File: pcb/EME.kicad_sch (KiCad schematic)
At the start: 42 parts, among them J1 BMP180, J10 INPUT ONLY, J11 UART0, J12 SPI_CONN, J13 UART0, J2 ReedSwitchX8, J3 SS41, J5 PanelSolar, J6 BH1750, J7 DHT22, J8 Baterias, J9 Jumper, U1 LM78M05_TO220, U5 TL082

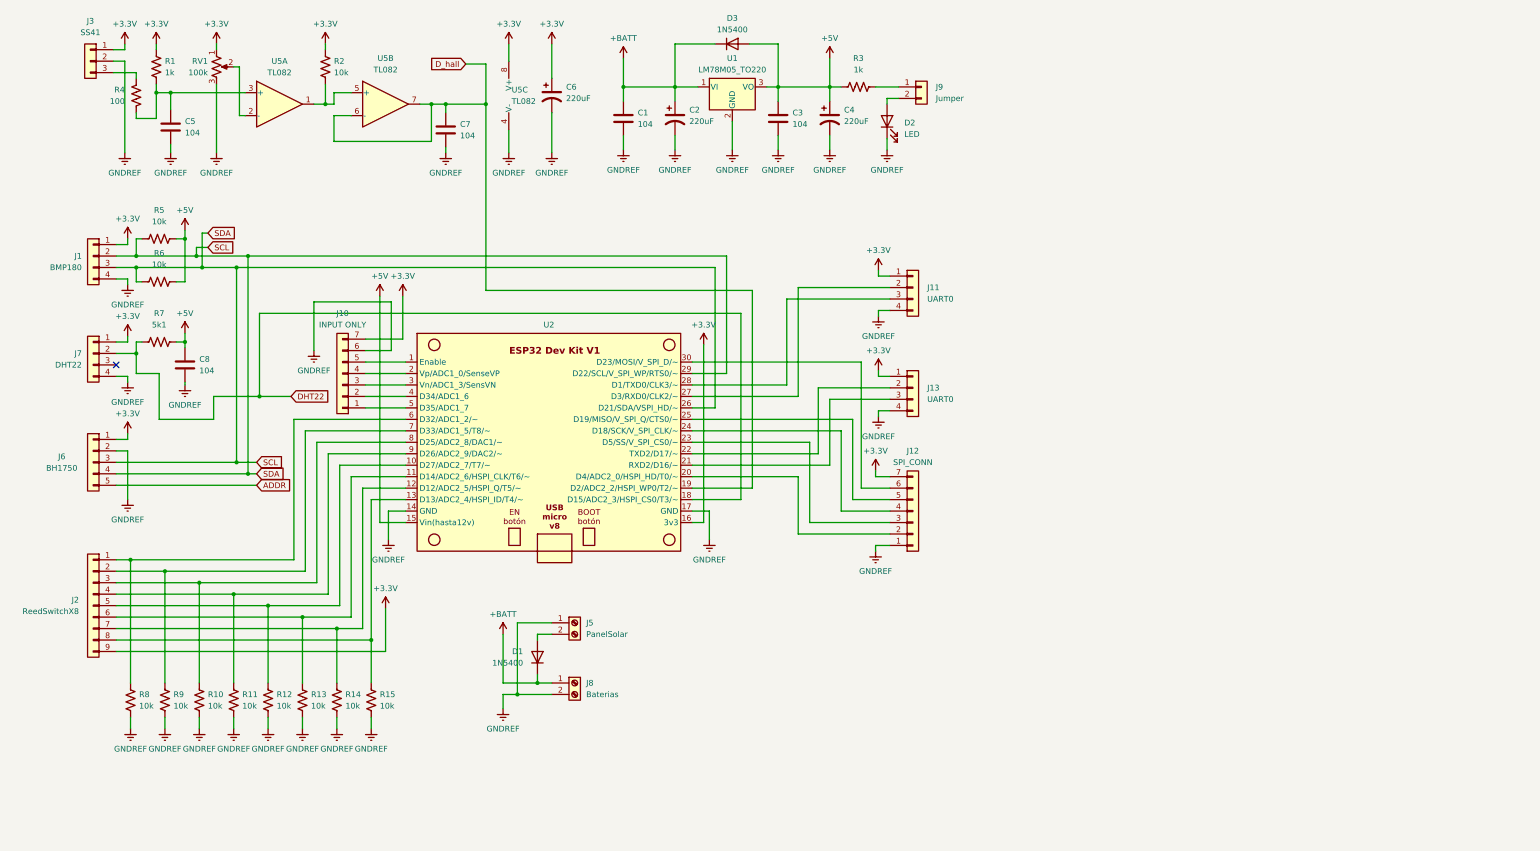
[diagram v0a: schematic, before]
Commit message: se agregaron ejemplos de los sensores y actualizo la PCB
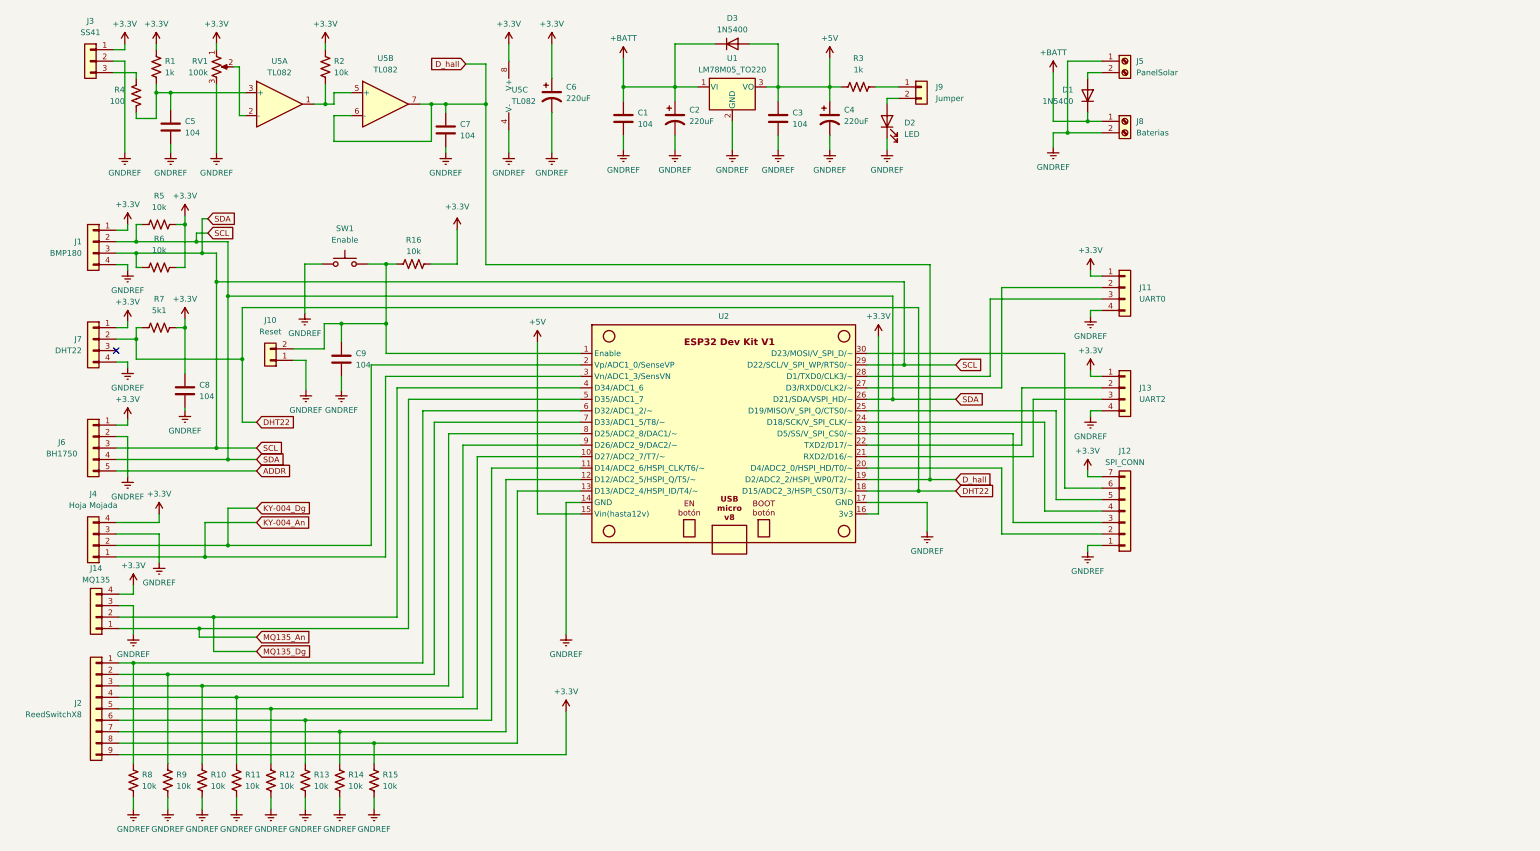
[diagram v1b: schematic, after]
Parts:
- removed J10: INPUT ONLY, Connector_PinHeader_2.54mm:PinHeader_1x07_P2.54mm_Vertical, symbol Connector_Generic:Conn_01x07
- added C9: 104, Capacitor_THT:C_Disc_D4.3mm_W1.9mm_P5.00mm, symbol Device:C
- added J10: Reset, Connector_PinHeader_2.54mm:PinHeader_1x02_P2.54mm_Vertical, symbol Connector_Generic:Conn_01x02
- added J14: MQ135, Connector_PinHeader_2.54mm:PinHeader_1x04_P2.54mm_Vertical, symbol Connector_Generic:Conn_01x04
- added J4: Hoja Mojada, Connector_PinHeader_2.54mm:PinHeader_1x04_P2.54mm_Vertical, symbol Connector_Generic:Conn_01x04
- added R16: 10k, Resistor_THT:R_Axial_DIN0207_L6.3mm_D2.5mm_P10.16mm_Horizontal, symbol Device:R_US
- added SW1: Enable, Button_Switch_THT:SW_PUSH_6mm_H8mm, symbol Switch:SW_Push
- J13: value UART0 -> UART2
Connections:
- net +3.3V: now also C8.1, R5.2, R6.2, R7.2, J14.4 (Pin_4), J4.4 (Pin_4), R16.1
- net +5V: no longer C8.1, R5.2, R6.2, R7.2
- net GNDREF: now also C9.2, J10.1 (Pin_1), J14.3 (Pin_3), J4.3 (Pin_3), SW1.1
- net at U2.1 (Enable): now also C9.1, J10.2 (Pin_2), R16.2, SW1.2
- net KY-004_Dg: now reaches U2.2 (Vp/ADC1_0/SenseVP)
- net KY-004_Dg: now also J4.2 (Pin_2)
- net KY-004_An: now reaches U2.3 (Vn/ADC1_3/SensVN)
- net KY-004_An: now also J4.1 (Pin_1)
- net MQ135_Dg: now reaches U2.4 (D34/ADC1_6)
- net MQ135_Dg: now also J14.2 (Pin_2)
- net MQ135_An: now reaches U2.5 (D35/ADC1_7)
- net MQ135_An: now also J14.1 (Pin_1)
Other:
- company: (none) -> ETec UM (Escuela Técnica de la Universidad de Mendoza)
- title: (none) -> Main Board EME (Estación Meteorológica Estática)
- moved on the sheet: C8, D1, J1, J11, J12, J13, J2, J5, J6, J7, J8, R10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

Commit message: Se armó diseño de PCB y se decoró esquemático
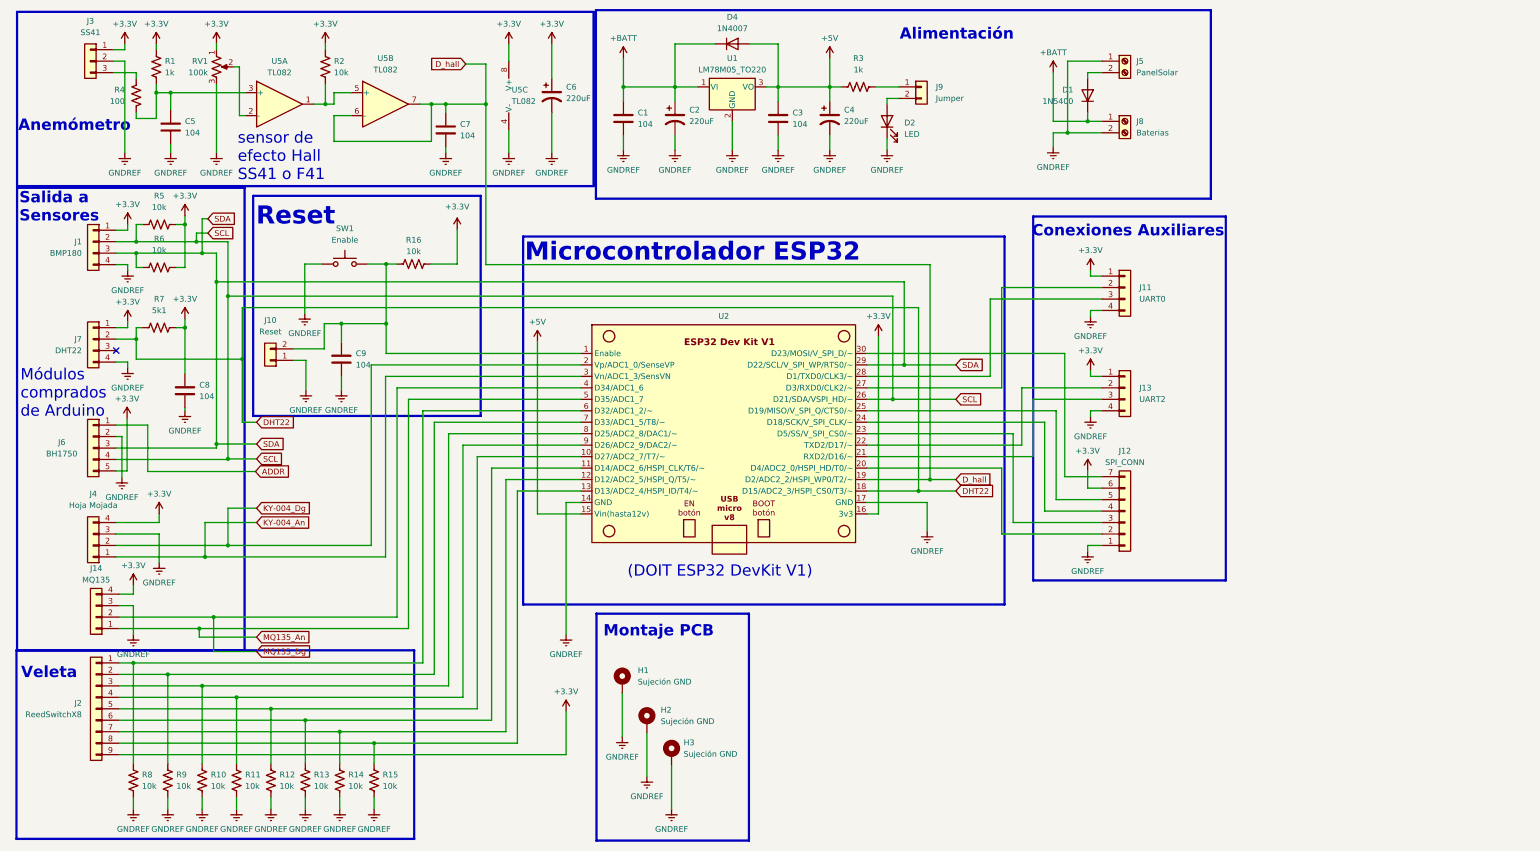
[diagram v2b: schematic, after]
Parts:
- removed D3: 1N5400, Diode_THT:D_DO-201AD_P15.24mm_Horizontal, symbol Diode:1N5400
- added D4: 1N4007, Diode_THT:D_DO-41_SOD81_P10.16mm_Horizontal, symbol Diode:1N4007
- added H1, H2, H3: Sujeción GND, MountingHole:MountingHole_3.2mm_M3_Pad_Via, symbol Mechanical:MountingHole_Pad_MP
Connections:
- net +3.3V: now also J12.6 (Pin_6), J6.5 (Pin_5); no longer J12.7 (Pin_7), J6.1 (Pin_1)
- net +5V: now also D4.2 (A)
- net +BATT: now also D4.1 (K)
- net ADDR: now also J6.1 (Pin_1); no longer J6.5 (Pin_5)
- net GNDREF: now also H1.MP, H2.MP, H3.MP
- net SCL: no longer J1.3 (Pin_3), J6.3 (Pin_3), R6.1, U2.29 (D22/SCL/V_SPI_WP/RTS0/~)
- net at U2.30 (D23/MOSI/V_SPI_D/~): now also J12.7 (Pin_7); no longer J12.6 (Pin_6)
- new net SDA: J1.3 (Pin_3), J6.3 (Pin_3), R6.1, U2.29 (D22/SCL/V_SPI_WP/RTS0/~)
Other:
- note added: "(DOIT ESP32 DevKit V1)"
- note added: "Alimentación"
- note added: "Anemómetro"
- note added: "Conexiones Auxiliares"
- note added: "Microcontrolador ESP32"
- note added: "Montaje PCB"
- note added: "Módulos comprados de Arduino"
- note added: "Reset"
- note added: "Salida a Sensores"
- note added: "Veleta"
- note added: "sensor de efecto Hall SS41 o F41"
- company: ETec UM (Escuela Técnica de la Universidad de Mendoza) -> ETec UM (Escuela Técnica de la Universidad de Mendoza).

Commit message: Add files via upload
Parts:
- removed J2: ReedSwitchX8, Connector_PinHeader_2.54mm:PinHeader_1x09_P2.54mm_Vertical, symbol Connector_Generic:Conn_01x09
- removed R10, R11, R12, R13, R14, R15, R8, R9: 10k, Resistor_THT:R_Axial_DIN0207_L6.3mm_D2.5mm_P10.16mm_Horizontal, symbol Device:R_US
- added J15: AS5600, Connector_PinHeader_2.54mm:PinHeader_1x05_P2.54mm_Vertical, symbol Connector_Generic:Conn_01x05
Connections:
- net +3.3V: now also J15.4 (Pin_4)
- net GNDREF: now also J15.5 (Pin_5)
- net SCL: now also J1.3 (Pin_3), J6.3 (Pin_3), R6.1, U2.29 (D22/SCL/V_SPI_WP/RTS0/~), J15.3 (Pin_3); no longer J1.2 (Pin_2), J6.4 (Pin_4), R5.1, U2.26 (D21/SDA/VSPI_HD/~)
- net SDA: now also J1.2 (Pin_2), J6.4 (Pin_4), R5.1, U2.26 (D21/SDA/VSPI_HD/~), J15.2 (Pin_2); no longer J1.3 (Pin_3), J6.3 (Pin_3), R6.1, U2.29 (D22/SCL/V_SPI_WP/RTS0/~)
- net at U2.6 (D32/ADC1_2/~): now also J15.1 (Pin_1)
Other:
- moved on the sheet: C1, C2, C3, C4, C5, C6, C7, C9, D1, D2, D4, H1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

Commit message: se actualizó la PCB
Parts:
- removed J11: UART0, Connector_PinHeader_2.54mm:PinHeader_1x04_P2.54mm_Vertical, symbol Connector_Generic:Conn_01x04
- removed J13: UART2, Connector_PinHeader_2.54mm:PinHeader_1x04_P2.54mm_Vertical, symbol Connector_Generic:Conn_01x04
- removed J15: AS5600, Connector_PinHeader_2.54mm:PinHeader_1x05_P2.54mm_Vertical, symbol Connector_Generic:Conn_01x05
- added D3: LED, LED_THT:LED_D5.0mm_Clear, symbol Device:LED
- added H4: Sujeción, MountingHole:MountingHole_3.2mm_M3_Pad_Via, symbol Mechanical:MountingHole_Pad_MP
- added J11: UART2, Connector_PinHeader_2.54mm:PinHeader_1x05_P2.54mm_Vertical, symbol Connector_Generic:Conn_01x05
- added J13: UART0, Connector_PinHeader_2.54mm:PinHeader_1x05_P2.54mm_Vertical, symbol Connector_Generic:Conn_01x05
- added J16: OUT, Connector_PinHeader_2.54mm:PinHeader_1x03_P2.54mm_Vertical, symbol Connector_Generic:Conn_01x03
- added J17: OE, Connector_PinHeader_2.54mm:PinHeader_1x03_P2.54mm_Vertical, symbol Connector_Generic:Conn_01x03
- added J18: GPIO's, Connector_PinHeader_2.54mm:PinHeader_1x05_P2.54mm_Vertical, symbol Connector_Generic:Conn_01x05
- added J19: I2C, Connector_PinHeader_2.54mm:PinHeader_1x05_P2.54mm_Vertical, symbol Connector_Generic:Conn_01x05
- added J2: ReedSwitchX8, Connector_PinHeader_2.54mm:PinHeader_1x09_P2.54mm_Vertical, symbol Connector_Generic:Conn_01x09
- added J20: Jumper, Connector_PinHeader_2.54mm:PinHeader_1x02_P2.54mm_Vertical, symbol Connector_Generic:Conn_01x02
- added Q1, Q2: IRF540N, Package_TO_SOT_THT:TO-220-3_Vertical, symbol Transistor_FET:IRF540N
- added R10, R11, R12, R13, R14, R15, R8, R9: 10k, Resistor_THT:R_Axial_DIN0207_L6.3mm_D2.5mm_P10.16mm_Horizontal, symbol Device:R_US
- added R17, R20, R24: 1k, Resistor_THT:R_Axial_DIN0207_L6.3mm_D2.5mm_P10.16mm_Horizontal, symbol Device:R_US
- added R18, R19, R21, R22, R23: 4k7, Resistor_THT:R_Axial_DIN0207_L6.3mm_D2.5mm_P10.16mm_Horizontal, symbol Device:R_US
- added U3: 74HC251, Package_DIP:DIP-16_W7.62mm_LongPads, symbol Connector_Generic:Conn_02x08_Counter_Clockwise
- H1, H2, H3: value Sujeción GND -> Sujeción
- J5: footprint TerminalBlock_Phoenix:TerminalBlock_Phoenix_MPT-0,5-2-2.54_1x02_P2.54mm_Horizontal -> TerminalBlock_Phoenix:TerminalBlock_Phoenix_PT-1,5-2-3.5-H_1x02_P3.50mm_Horizontal
- J8: footprint TerminalBlock_Phoenix:TerminalBlock_Phoenix_MPT-0,5-2-2.54_1x02_P2.54mm_Horizontal -> TerminalBlock_Phoenix:TerminalBlock_Phoenix_PT-1,5-2-5.0-H_1x02_P5.00mm_Horizontal
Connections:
- net +3.3V: now also J12.7 (Pin_7), R16.2, J11.5 (Pin_5), J13.5 (Pin_5), J17.3 (Pin_3), J18.1 (Pin_1), J19.4 (Pin_4), U3.16 (Pin_16); no longer J12.6 (Pin_6), R16.1
- net +5V: now also J12.6 (Pin_6), J11.4 (Pin_4), J13.4 (Pin_4), J19.5 (Pin_5)
- net +BATT: now also R24.1
- net GNDREF: now also D3.1 (K), H4.MP, Q1.3 (S), Q2.3 (S), R18.1, R19.1; no longer C5.2, C6.2, C7.2, J1.4 (Pin_4), J12.1 (Pin_1), J14.3 (Pin_3), J3.2 (Pin_2), J4.3 (Pin_3), J6.2 (Pin_2), J7.4 (Pin_4), RV1.3, U5.4 (V-)
- net SCL: now also J1.2 (Pin_2), J6.4 (Pin_4), R5.1, J19.3 (Pin_3); no longer J1.3 (Pin_3), J6.3 (Pin_3), R6.1
- net SDA: now also J1.3 (Pin_3), J6.3 (Pin_3), R6.1, J19.2 (Pin_2); no longer J1.2 (Pin_2), J6.4 (Pin_4), R5.1
- net GPIO4: now reaches U2.20 (D4/ADC2_0/HSPI_HD/T0/~)
- net GPIO4: now also J18.4 (Pin_4), R23.2; no longer J12.2 (Pin_2)
- net MOSI: now reaches J12.3 (Pin_3)
- net MOSI: now also U2.30 (D23/MOSI/V_SPI_D/~); no longer U2.23 (D5/SS/V_SPI_CS0/~)
- net MISO: now reaches J12.4 (Pin_4)
- net MISO: now also U2.25 (D19/MISO/V_SPI_Q/CTS0/~); no longer U2.24 (D18/SCK/V_SPI_CLK/~)
- net GND_G2: now reaches J12.5 (Pin_5)
- net GND_G2: now also J11.1 (Pin_1), J13.1 (Pin_1), J18.5 (Pin_5), J19.1 (Pin_1), Q2.2 (D), R21.1, R22.1, R23.1; no longer U2.25 (D19/MISO/V_SPI_Q/CTS0/~)
- net at C5.1, R1.2, U5.3 (+): now also R4.1; no longer R4.2
- net Rest: now reaches C9.1, J10.2 (Pin_2), SW1.2, U2.1 (Enable)
- net Rest: now also R16.1; no longer R16.2
- net RX0: now reaches U2.27 (D3/RXD0/CLK2/~)
- net RX0: now also J13.2 (Pin_2)
- net TX0: now reaches U2.28 (D1/TXD0/CLK3/~)
- net TX0: now also J13.3 (Pin_3)
- net at J3.3 (Pin_3): now also R4.2; no longer R4.1
- net G2: now reaches U2.10 (D27/ADC2_7/T7/~)
- net G2: now also R20.2
- net G1: now reaches U2.11 (D14/ADC2_6/HSPI_CLK/T6/~)
- net G1: now also R17.2
- net GPIO12: now reaches U2.12 (D12/ADC2_5/HSPI_Q/T5/~)
- net GPIO12: now also J18.2 (Pin_2), R21.2
- net GPIO13: now reaches U2.13 (D13/ADC2_4/HSPI_ID/T4/~)
- net GPIO13: now also J18.3 (Pin_3), R22.2
- net RX2: now reaches U2.21 (RXD2/D16/~)
- net RX2: now also J11.2 (Pin_2)
- net TX2: now reaches U2.22 (TXD2/D17/~)
- net TX2: now also J11.3 (Pin_3)
- net S0: now reaches U2.6 (D32/ADC1_2/~)
- net S0: now also U3.11 (Pin_11)
- net S1: now reaches U2.7 (D33/ADC1_5/T8/~)
- net S1: now also U3.10 (Pin_10)
- net S2: now reaches U2.8 (D25/ADC2_8/DAC1/~)
- net S2: now also U3.9 (Pin_9)
- net Y: now reaches U2.9 (D26/ADC2_9/DAC2/~)
- net Y: now also J16.2 (Pin_2)
- new net: J2.3 (Pin_3), R10.1, U3.14 (Pin_14)
- new net: Q1.1 (G), R17.1, R18.2
- new net: J2.4 (Pin_4), R11.1, U3.15 (Pin_15)
- new net: J2.8 (Pin_8), R15.1, U3.4 (Pin_4)
- new net: J2.2 (Pin_2), R9.1, U3.13 (Pin_13)
- new net: J2.6 (Pin_6), R13.1, U3.2 (Pin_2)
- new net: J2.1 (Pin_1), R8.1, U3.12 (Pin_12)
- new net: Q2.1 (G), R19.2, R20.1
- new net: J2.7 (Pin_7), R14.1, U3.3 (Pin_3)
- new net: J20.1 (Pin_1), R24.2
- new net: D3.2 (A), J20.2 (Pin_2)
- new net: J2.5 (Pin_5), R12.1, U3.1 (Pin_1)
- new net: J16.1 (Pin_1), U3.5 (Pin_5)
- new net: J16.3 (Pin_3), U3.6 (Pin_6)
- new net: J17.2 (Pin_2), U3.7 (Pin_7)
- new net GND_G1: C5.2, C6.2, C7.2, J1.4 (Pin_4), J14.3 (Pin_3), J17.1 (Pin_1), J2.9 (Pin_9), J3.2 (Pin_2), J4.3 (Pin_3), J6.2 (Pin_2), J7.4 (Pin_4), Q1.2 (D), R10.2, R11.2, R12.2, R13.2, R14.2, R15.2, R8.2, R9.2, RV1.3, U3.8 (Pin_8), U5.4 (V-)
- new net SCK: J12.2 (Pin_2), U2.24 (D18/SCK/V_SPI_CLK/~)
- new net SS: J12.1 (Pin_1), U2.23 (D5/SS/V_SPI_CS0/~)
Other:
- note added: "Cada Bus de "GND_Gx" es usado para poder alimentar o dejar de alimentar los sensores o conjunto de los mismos"
- note added: "El microcontrolador ESP32 en su placa de desarrollo de 30 terminales de conexión, modelo <DOIT DevKit V1> es el que se implementa en este proyecto, contemplando que sus GPIO mayormente funcionan con 3v3 se decidió por colocar un módulo level shiffter de 8 canales para las comunicaciones externas, cómo GPS, GRMS, LCD(5v), lector uSD, etc."
- note added: "GND Gx"
- moved on the sheet: C1, C2, C3, C4, C5, C6, C7, C8, C9, D1, D2, D4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

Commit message: se actualizó la PCB
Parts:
- J5: footprint TerminalBlock_Phoenix:TerminalBlock_Phoenix_PT-1,5-2-3.5-H_1x02_P3.50mm_Horizontal -> TerminalBlock_Phoenix:TerminalBlock_Phoenix_PT-1,5-2-5.0-H_1x02_P5.00mm_Horizontal
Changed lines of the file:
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@@
 			)
 		)
-		(property "Footprint" "TerminalBlock_Phoenix:TerminalBlock_Phoenix_PT-1,5-2-3.5-H_1x02_P3.50mm_Horizontal"
+		(property "Footprint" "TerminalBlock_Phoenix:TerminalBlock_Phoenix_PT-1,5-2-5.0-H_1x02_P5.00mm_Horizontal"
 			(at 245.11 25.4 0)
 			(effects
